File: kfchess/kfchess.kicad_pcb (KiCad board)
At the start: 2 copper layers, 232 parts, among them Q1 AO3400A, Q10 AO3400A, Q11 AO3400A, Q12 AO3400A, Q13 AO3400A, Q14 AO3400A, Q15 AO3400A, Q16 AO3400A, Q2 AO3400A, Q3 AO3400A, Q4 AO3400A, Q5 AO3400A, Q6 AO3400A, Q7 AO3400A, Q8 AO3400A, Q9 AO3400A, U1 XY308-2_54-2P, U2 XY308-2_54-2P, U3 XY308-2_54-2P, U4 Teensy4.1, U5 XY308-2_54-8P, U6 XY308-2_54-8P, U7 XY308-2_54-8P, U8 XY308-2_54-8P

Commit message: Fixed holes
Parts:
- U1, U2, U3, U4, U5, U6, U7, U8: moved to B.Cu
- moved U8 139.8 mm to (300.0, 231.7), turned to 90 degrees
- moved U7 124.4 mm to (300.0, 207.6), turned to 90 degrees
- moved U5 117.5 mm to (300.0, 159.7), turned to 90 degrees
- moved U6 116.6 mm to (300.0, 183.8), turned to 90 degrees
- moved U4 11.3 mm to (292.6, 61.2), turned to -90 degrees
- moved U1 2.50 mm to (300.0, 116.7), turned to 90 degrees
- moved U2 2.50 mm to (300.0, 128.0), turned to 90 degrees
- moved U3 2.50 mm to (300.0, 139.2), turned to 90 degrees
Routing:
- net /row4/square4/em_n: track 0.00 -> 63.0 mm
- added copper zone on B.Cu, net GND
- added copper zone on F.Cu, net GND
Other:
- board outline added: 260 x 220 mm

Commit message: Started routing
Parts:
- moved D4 36.0 mm to (67.0, 65.0), turned to 90 degrees
- moved D8 36.0 mm to (103.0, 65.0), turned to -90 degrees
- moved D102 33.3 mm to (222.3, 152.3), turned to 45 degrees
- moved D111 33.3 mm to (72.3, 202.3), turned to 45 degrees
- moved D12 33.3 mm to (122.3, 52.3), turned to 45 degrees
- moved D120 33.3 mm to (122.3, 202.3), turned to 45 degrees
- moved D129 33.3 mm to (172.3, 202.3), turned to 45 degrees
- moved D138 33.3 mm to (222.3, 202.3), turned to 45 degrees
- moved D21 33.3 mm to (172.3, 52.3), turned to 45 degrees
- moved D30 33.3 mm to (222.3, 52.3), turned to 45 degrees
- moved D39 33.3 mm to (72.3, 102.3), turned to 45 degrees
- moved D48 33.3 mm to (122.3, 102.3), turned to 45 degrees
- moved D57 33.3 mm to (172.3, 102.3), turned to 45 degrees
- moved D66 33.3 mm to (222.3, 102.3), turned to 45 degrees
- moved D75 33.3 mm to (72.3, 152.3), turned to 45 degrees
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- renumbered D103 to D102, D105 to D103, D107 to D104, D102 to D105, D104 to D106, D106 to D107, D112 to D111, D114 to D112, D116 to D113, D111 to D114, D113 to D115, D115 to D116, D13 to D12, D121 to D120, D123 to D121, D125 to D122, D120 to D123, D122 to D124, D124 to D125, D130 to D129, D15 to D13, D132 to D130, D134 to D131, D129 to D132, D131 to D133, D133 to D134, D139 to D138, D141 to D139, D17 to D14, D143 to D140, D138 to D141, D140 to D142, D142 to D143, D12 to D15, D14 to D16, D16 to D17, D22 to D21, D24 to D22, D26 to D23, D21 to D24, D23 to D25, D25 to D26, D31 to D30, D33 to D31, D35 to D32, D30 to D33, D32 to D34, D34 to D35, D40 to D39, D42 to D40, D44 to D41, D39 to D42, D41 to D43, D43 to D44, D49 to D48, D51 to D49, D53 to D50, D48 to D51, D50 to D52, D52 to D53, D58 to D57, D60 to D58, D62 to D59, D57 to D60, D59 to D61, D61 to D62, D67 to D66, D69 to D67, D71 to D68, D66 to D69, D68 to D70, D70 to D71, D76 to D75, D78 to D76, D80 to D77, D75 to D78, D77 to D79, D79 to D80, D85 to D84, D87 to D85, D89 to D86, D84 to D87, D86 to D88, D88 to D89, D94 to D93, D96 to D94, D98 to D95, D93 to D96, D95 to D97, D97 to D98, U4 to U2, U2 to U3, U3 to U4
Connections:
- D3 pad 3: Net-(D3-DIN) -> Net-(D2-DOUT)
- D4 pad 3: Net-(D2-DOUT) -> Net-(D3-DOUT)
- D5 pad 3: Net-(D3-DOUT) -> Net-(D4-DOUT)
- D6 pad 3: Net-(D4-DOUT) -> Net-(D5-DOUT)
- D7 pad 3: Net-(D5-DOUT) -> Net-(D6-DOUT)
- D8 pad 1: Net-(D3-DIN) -> Net-(D8-DOUT)
- D8 pad 3: Net-(D6-DOUT) -> Net-(D7-DOUT)
- D9 pad 3: Net-(D7-DOUT) -> Net-(D8-DOUT)
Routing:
- net +5V: track 0.00 -> 1169.3 mm
- net /s11: track 0.00 -> 68.4 mm
- net /s32: track 0.00 -> 51.1 mm
- net /s44: track 0.00 -> 51.1 mm
- net /s43: track 0.00 -> 51.1 mm
- net /s42: track 0.00 -> 51.1 mm
- net /s41: track 0.00 -> 51.1 mm
- net /s34: track 0.00 -> 51.1 mm
- net /s33: track 0.00 -> 51.1 mm
- net /s22: track 0.00 -> 51.1 mm
- net /s31: track 0.00 -> 51.1 mm
- net /s24: track 0.00 -> 51.1 mm
- net /s23: track 0.00 -> 51.1 mm
- net /s21: track 0.00 -> 51.1 mm
- net /s12: track 0.00 -> 51.1 mm
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
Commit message: More routing
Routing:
- net +5V: track 1169.3 -> 2243.8 mm
- net +5V_em: track 30.2 -> 336.6 mm, vias 0 -> 1
- net /leds: track 0.00 -> 233.9 mm, vias 0 -> 1
- net /s11: track 68.4 -> 237.0 mm, vias 0 -> 1
- net /c11: track 33.9 -> 191.1 mm
- net /s12: track 51.1 -> 189.4 mm, vias 0 -> 1
- net Net-(Q2-G): track 9.09 -> 146.6 mm
- net /s13: track 51.1 -> 138.2 mm, vias 0 -> 1
- net Net-(Q3-G): track 9.09 -> 96.2 mm
- net /s14: track 51.1 -> 88.0 mm, vias 0 -> 1
- net Net-(Q4-G): track 9.09 -> 45.8 mm
- net Net-(D80-DOUT): track 16.7 -> 27.5 mm
- net Net-(D89-DOUT): track 16.7 -> 27.5 mm
- net Net-(D143-DOUT): track 16.7 -> 27.5 mm
- net Net-(D134-DOUT): track 16.7 -> 27.5 mm
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
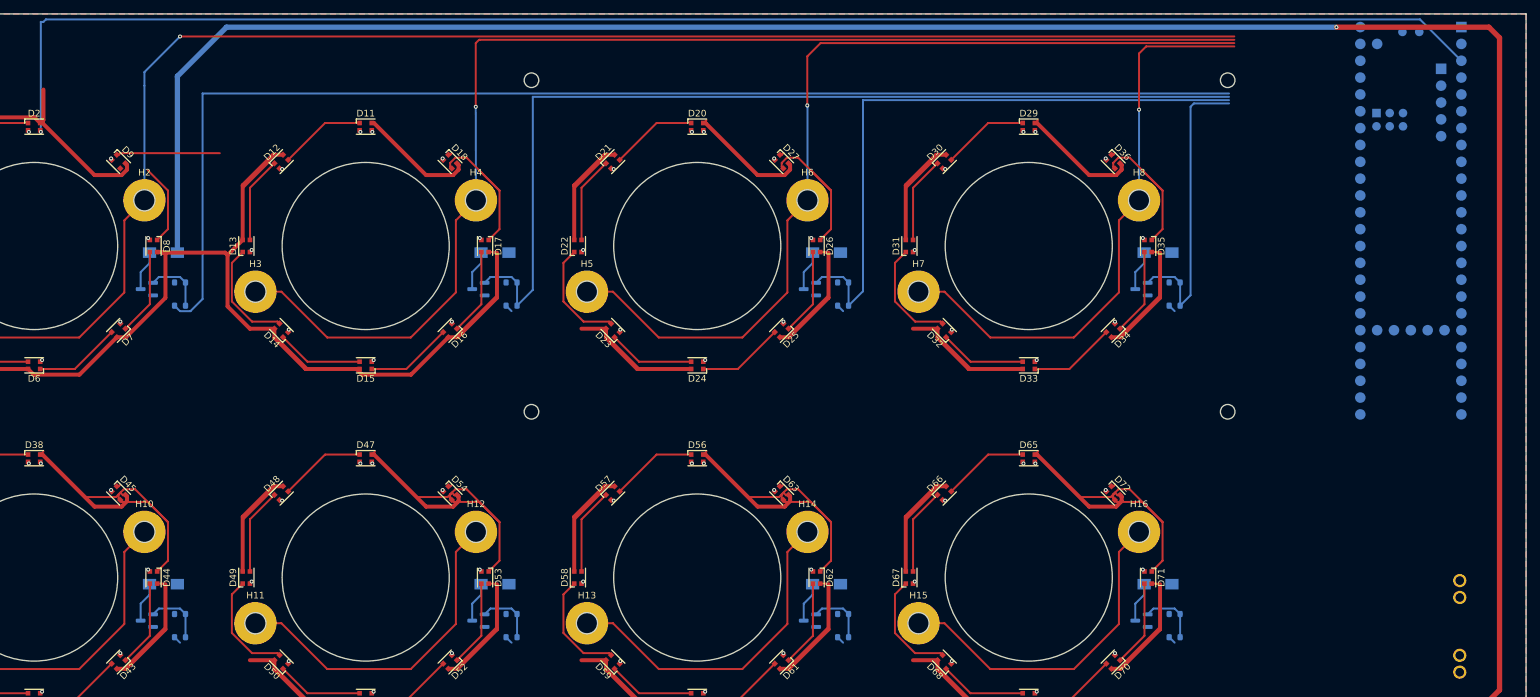
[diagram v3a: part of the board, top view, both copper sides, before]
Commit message: Finished routing top squares
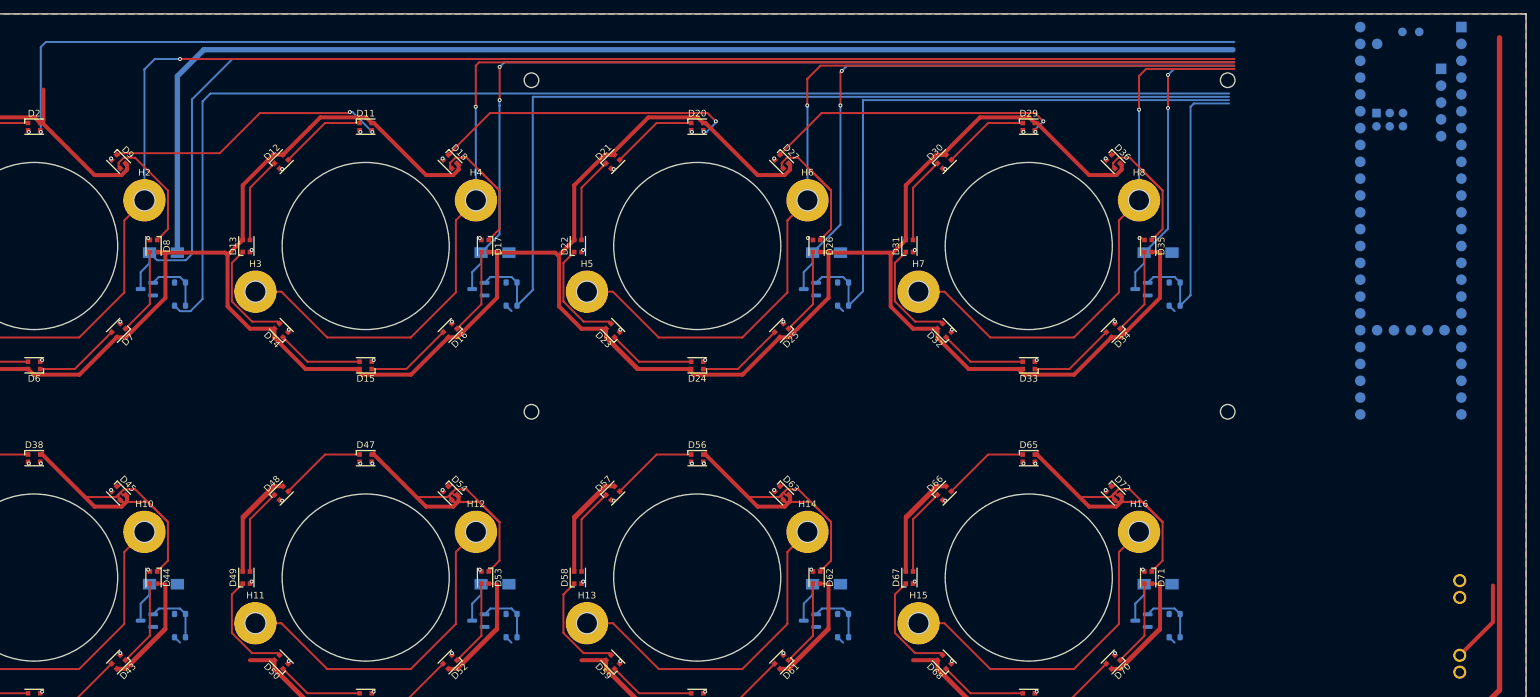
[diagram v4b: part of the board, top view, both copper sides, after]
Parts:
- renumbered U3 to U2, U4 to U3, U2 to U4
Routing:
- net /row1/square1/em_n: track 6.05 -> 196.4 mm
- net /row1/square2/em_n: track 6.05 -> 146.3 mm, vias 0 -> 2
- net /row1/square3/em_n: track 6.05 -> 94.9 mm, vias 0 -> 2
- net /row1/square2/d_out: track 0.91 -> 47.0 mm, vias 1 -> 2
- net /row1/square3/d_out: track 0.91 -> 45.5 mm, vias 1 -> 2
- net +5V_em: track 336.6 -> 294.3 mm, vias 1 -> 0
- net /leds: track 233.9 -> 193.4 mm
- net /row1/square4/em_n: track 6.05 -> 44.7 mm, vias 0 -> 2
- net /row1/square1/d_out: track 15.9 -> 42.7 mm, vias 1 -> 2
- net +5V: track 2243.8 -> 2258.1 mm
- net Net-(D8-DOUT): track 12.4 -> 18.9 mm
- net /s14: track 88.0 -> 84.6 mm
- net /s13: track 138.2 -> 134.8 mm
- net /s12: track 189.4 -> 186.0 mm
- net /s11: track 237.0 -> 235.8 mm
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
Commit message: Actually finished top
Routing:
- net +5V: track 2258.1 -> 574.8 mm
- net /c12: track 1.17 -> 140.6 mm
- net Net-(Q2-G): track 146.6 -> 9.09 mm
- net +5V_em: track 294.3 -> 398.3 mm, vias 0 -> 6
- net /c13: track 1.17 -> 90.2 mm
- net Net-(Q3-G): track 96.2 -> 9.09 mm
- net /s32: track 51.1 -> 0.00 mm
- net /s44: track 51.1 -> 0.00 mm
- net /s43: track 51.1 -> 0.00 mm
- net /s42: track 51.1 -> 0.00 mm
- net /s41: track 51.1 -> 0.00 mm
- net /s34: track 51.1 -> 0.00 mm
- net /s33: track 51.1 -> 0.00 mm
- net /s22: track 51.1 -> 0.00 mm
- net /s31: track 51.1 -> 0.00 mm
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
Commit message: Copied routing for bottom squares
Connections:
- R25 pad 2: /c31 -> /c41
- R27 pad 2: /c32 -> /c42
- R29 pad 2: /c33 -> /c43
- R31 pad 2: /c34 -> /c44
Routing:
- net +5V: track 574.8 -> 2249.0 mm
- net +5V_em: track 398.3 -> 1644.8 mm, vias 6 -> 25
- net /s41: track 0.00 -> 235.9 mm, vias 0 -> 1
- net /s21: track 0.00 -> 235.9 mm, vias 0 -> 1
- net /s31: track 0.00 -> 235.9 mm, vias 0 -> 1
- net /row2/d_out: track 0.00 -> 212.2 mm, vias 0 -> 2
- net /row3/d_out: track 0.00 -> 211.1 mm, vias 0 -> 2
- net /row3/square1/em_n: track 0.00 -> 201.5 mm
- net /row4/square1/em_n: track 0.00 -> 201.5 mm
- net /row2/square1/em_n: track 0.00 -> 201.5 mm
- net /c41: track 0.00 -> 190.4 mm
- net /c31: track 0.00 -> 190.4 mm
- net /c21: track 0.00 -> 190.4 mm
- net /s42: track 0.00 -> 187.0 mm, vias 0 -> 1
- net /s32: track 0.00 -> 187.0 mm, vias 0 -> 1
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
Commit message: Tentatively finished routing
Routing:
- net +5V: track 2249.0 -> 2713.4 mm, vias 0 -> 8
- net /row1/square4/em_n: track 44.9 -> 212.2 mm, vias 2 -> 3
- net /row1/square1/em_n: track 201.5 -> 366.6 mm, vias 0 -> 3
- net /row1/square3/em_n: track 96.9 -> 261.8 mm, vias 2 -> 3
- net /row1/square2/em_n: track 150.6 -> 314.1 mm, vias 2 -> 3
- net /row2/square4/em_n: track 44.9 -> 190.9 mm, vias 2 -> 5
- net /row2/square3/em_n: track 96.9 -> 238.6 mm, vias 2 -> 5
- net /row2/square2/em_n: track 150.6 -> 287.2 mm, vias 2 -> 5
- net /row2/square1/em_n: track 201.5 -> 334.0 mm, vias 0 -> 3
- net /s41: track 235.9 -> 362.1 mm, vias 1 -> 2
- net /s42: track 187.0 -> 311.4 mm, vias 1 -> 2
- net /c41: track 190.4 -> 314.0 mm, vias 0 -> 2
- net /s44: track 84.6 -> 207.8 mm, vias 1 -> 4
- net /c42: track 140.6 -> 261.0 mm, vias 0 -> 2
- net /s43: track 134.9 -> 253.6 mm, vias 1 -> 4
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
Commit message: Fixed errors
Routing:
- net Net-(U4-3_LRCLK2): track 0.00 -> 78.3 mm, vias 0 -> 1
- net Net-(U4-2_OUT2): track 0.00 -> 77.5 mm, vias 0 -> 1
- net +5V: track 2713.4 -> 2682.8 mm
- net Net-(D89-DOUT): track 23.2 -> 19.5 mm
- net Net-(D134-DOUT): track 23.2 -> 19.5 mm
- net Net-(D107-DOUT): track 23.2 -> 19.5 mm
- net Net-(D53-DOUT): track 23.2 -> 19.6 mm
- net Net-(D125-DOUT): track 23.2 -> 19.6 mm
- net Net-(D98-DOUT): track 23.2 -> 19.6 mm
- net Net-(D71-DOUT): track 23.2 -> 19.6 mm
- net Net-(D143-DOUT): track 23.2 -> 19.7 mm
- net Net-(D62-DOUT): track 23.2 -> 19.9 mm
- net /row4/square3/d_out: track 45.5 -> 46.5 mm
- net /c24: track 102.7 -> 103.3 mm
- net Net-(D80-DOUT): track 18.9 -> 19.5 mm
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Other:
- outline, holes or cut-outs redrawn
